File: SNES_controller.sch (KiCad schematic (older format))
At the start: 19 parts, among them J1 Conn_01x07, SW1 R, SW10 SELECT, SW11 Y, SW12 B, SW2 L, SW3 X, SW4 A, SW5 RIGHT, SW6 LEFT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

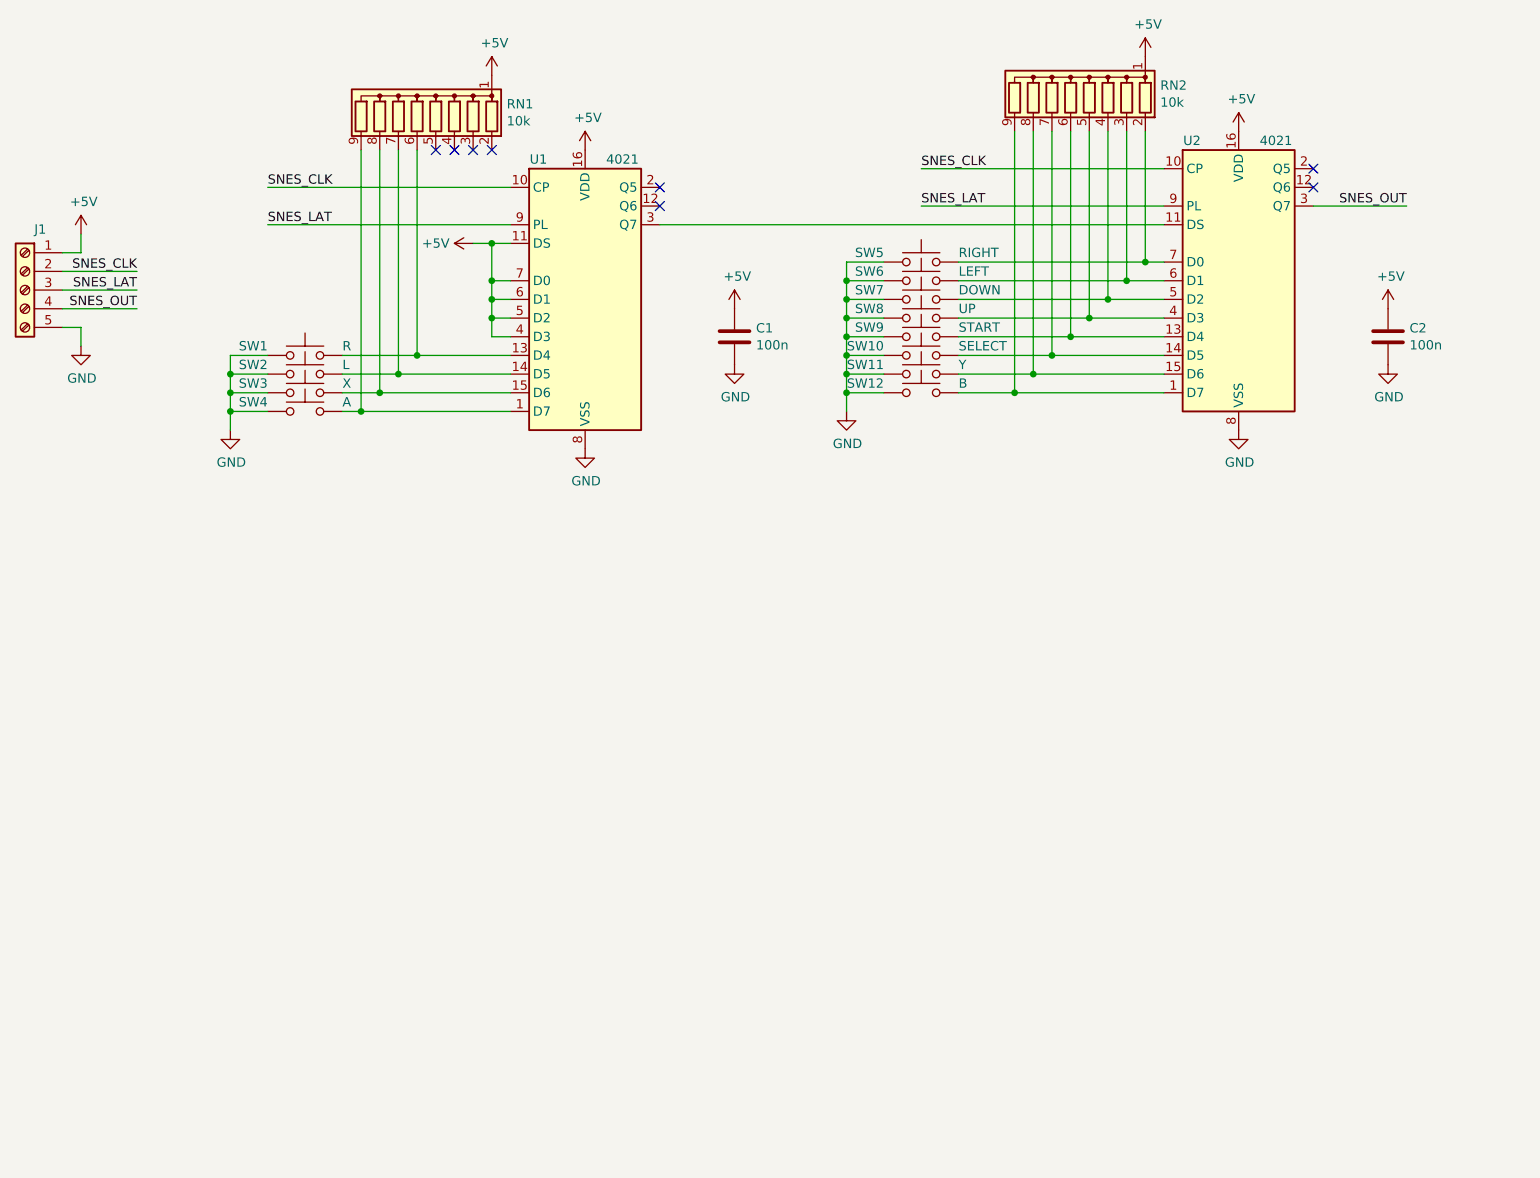
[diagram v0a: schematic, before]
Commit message: Change switches to connectors, add logic to prevent UP/DOWN or LEFT/RIGHT from being pressed simultaneously.
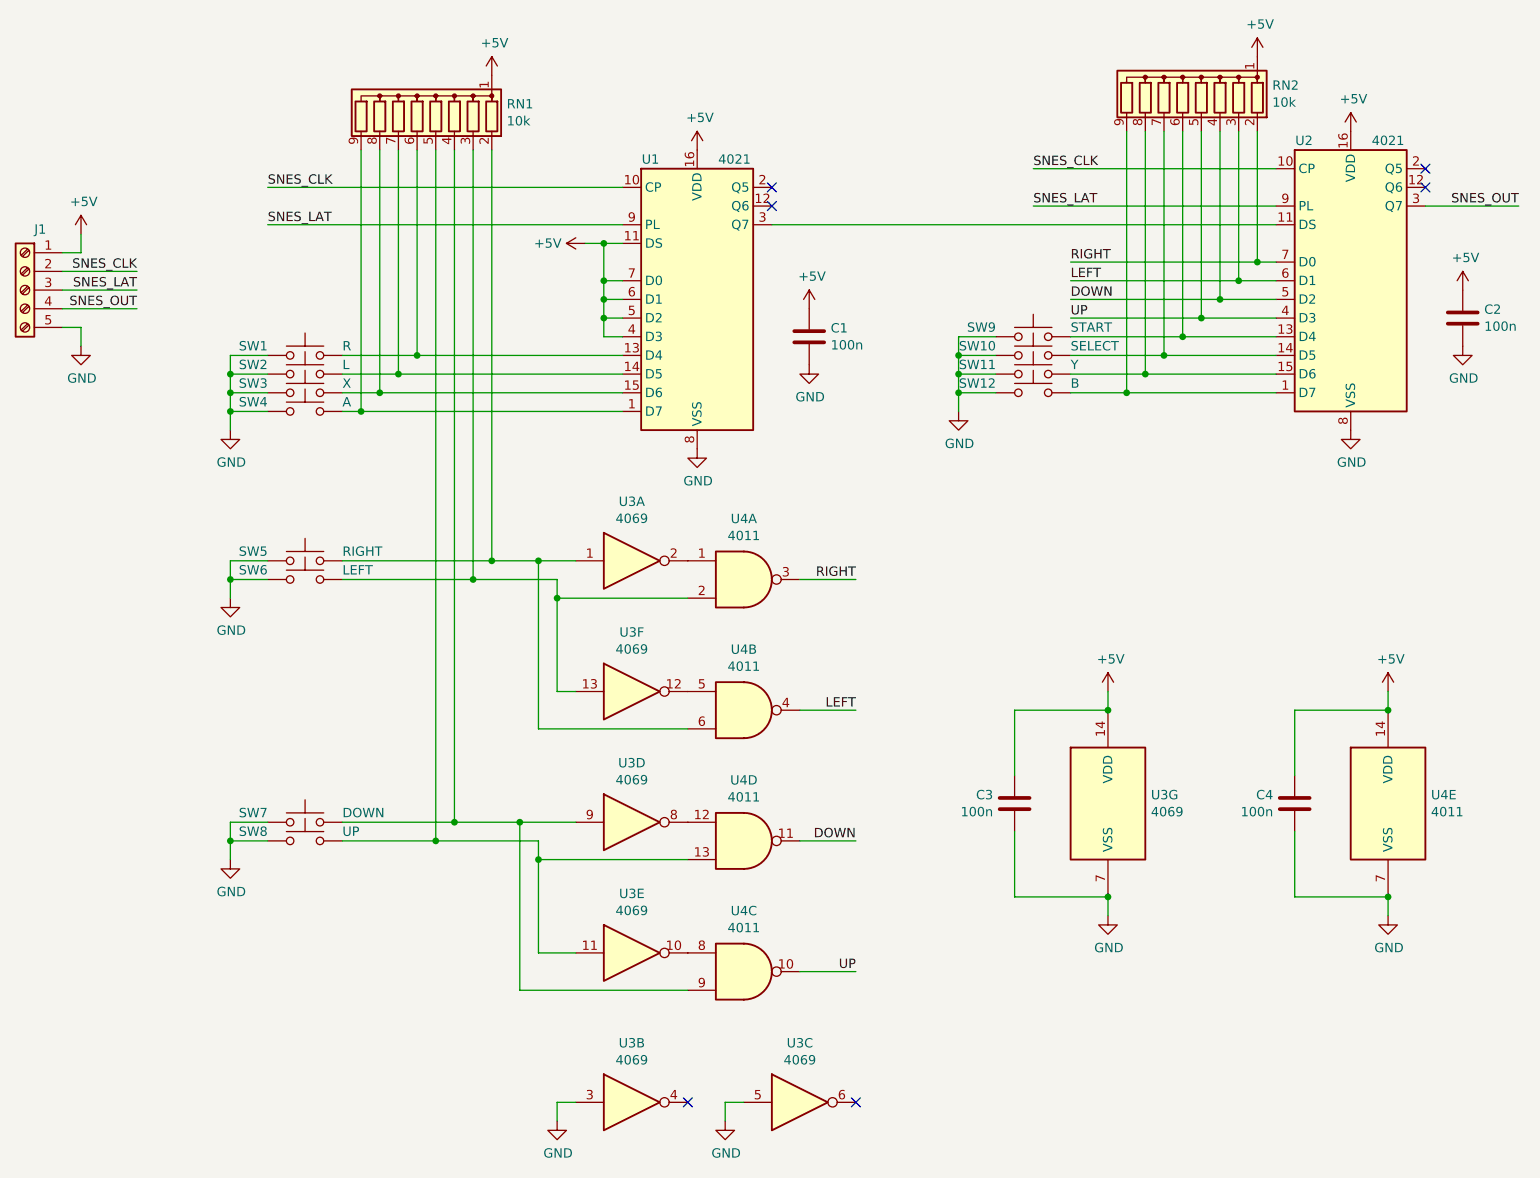
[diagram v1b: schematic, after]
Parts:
- added C3, C4: 100n, Capacitor_THT:C_Disc_D5.0mm_W2.5mm_P5.00mm, symbol Device:C
- added U3: 4069, Package_DIP:DIP-14_W7.62mm_Socket, symbol 4xxx:4069
- added U4: 4011, Package_DIP:DIP-14_W7.62mm_Socket, symbol 4xxx:4011
- J1: footprint Connector_Phoenix_MSTB:PhoenixContact_MSTBA_2,5_5-G-5,08_1x05_P5.08mm_Horizontal -> TerminalBlock_Phoenix:TerminalBlock_Phoenix_MKDS-1,5-5-5.08_1x05_P5.08mm_Horizontal
- SW1, SW2: footprint Button_Switch_THT:SW_Tactile_SKHH_Angled -> Connector_JST:JST_XH_B2B-XH-A_1x02_P2.50mm_Vertical
- SW10, SW11, SW12, SW3, SW4, SW5, SW6, SW7, SW8, SW9: footprint Button_Switch_THT:SW_PUSH_6mm_H8mm -> Connector_JST:JST_XH_B2B-XH-A_1x02_P2.50mm_Vertical
- U1, U2: footprint Package_DIP:DIP-16_W10.16mm -> Package_DIP:DIP-16_W7.62mm_Socket
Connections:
- net +5V: now also C3.1, C4.1, U3.14 (VDD), U4.14 (VDD)
- net GND: now also C3.2, C4.2, U3.3, U3.5, U3.7 (VSS), U4.7 (VSS)
- net UP: now reaches RN2.5 (R4), U2.4 (D3)
- net UP: now also U4.10; no longer SW8.2
- net DOWN: now reaches RN2.4 (R3), U2.5 (D2)
- net DOWN: now also U4.11; no longer SW7.2
- net LEFT: now reaches RN2.3 (R2), U2.6 (D1)
- net LEFT: now also U4.4; no longer SW6.2
- net RIGHT: now reaches RN2.2 (R1), U2.7 (D0)
- net RIGHT: now also U4.3; no longer SW5.2
- net at RN1.2 (R1): now also SW5.2, U3.1, U4.6
- net at RN1.3 (R2): now also SW6.2, U3.13, U4.2
- net at RN1.4 (R3): now also SW7.2, U3.9, U4.9
- net at RN1.5 (R4): now also SW8.2, U3.11, U4.13
- new net: U3.2, U4.1
- new net: U3.12, U4.5
- new net: U3.8, U4.12
- new net: U3.10, U4.8
- no-connect marks 8 -> 6
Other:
- moved on the sheet: C1, C2, RN2, SW10, SW11, SW12, SW5, SW6, SW7, SW8, SW9, U1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

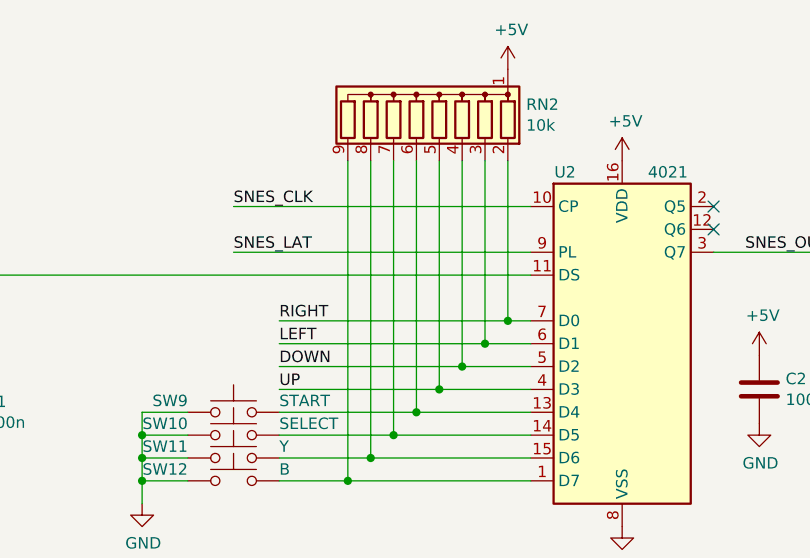
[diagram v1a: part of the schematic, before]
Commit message: Disconnect unnecessary pullups
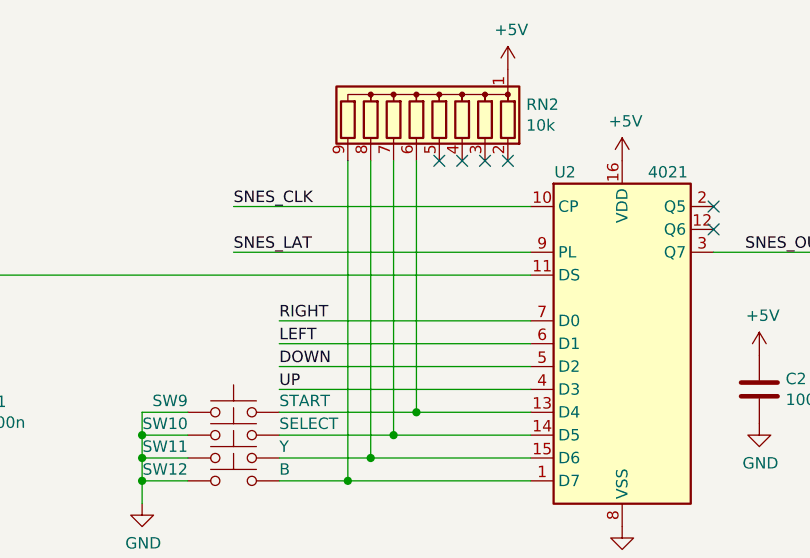
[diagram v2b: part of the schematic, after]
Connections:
- net DOWN: no longer RN2.4 (R3)
- net LEFT: no longer RN2.3 (R2)
- net RIGHT: no longer RN2.2 (R1)
- net UP: no longer RN2.5 (R4)
- no-connect marks 6 -> 10
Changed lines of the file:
@@
 $EndComp
-Wire Wire Line
-	8300 1900 8300 2600
-Wire Wire Line
-	8300 2600 8400 2600
-Wire Wire Line
-	8400 2700 8200 2700
-Wire Wire Line
-	8200 2700 8200 1900
-Wire Wire Line
-	8100 1900 8100 2800
-Wire Wire Line
-	8100 2800 8400 2800
-Wire Wire Line
-	8400 2900 8000 2900
-Wire Wire Line
-	8000 2900 8000 1900
 Wire Wire Line
 	7900 1900 7900 3000
@@
 	7300 3000 7900 3000
 Connection ~ 7900 3000
-Connection ~ 8000 2900
-Wire Wire Line
-	8100 2800 7300 2800
-Connection ~ 8100 2800
-Wire Wire Line
-	8200 2700 7300 2700
-Connection ~ 8200 2700
-Wire Wire Line
-	8300 2600 7300 2600
-Connection ~ 8300 2600
 $Comp
 L Switch:SW_Push SW7
@@
 	1    0    0    -1
 $EndComp
-Wire Wire Line
-	8000 2900 7300 2900
 $Comp
 L Switch:SW_Push SW8
@@
 	1    0    0    -1
 $EndComp
+Wire Wire Line
+	7300 2900 8400 2900
+Wire Wire Line
+	7300 2800 8400 2800
+Wire Wire Line
+	7300 2700 8400 2700
+Wire Wire Line
+	7300 2600 8400 2600
+NoConn ~ 8000 1900
+NoConn ~ 8100 1900
+NoConn ~ 8200 1900
+NoConn ~ 8300 1900
 $EndSCHEMATC
